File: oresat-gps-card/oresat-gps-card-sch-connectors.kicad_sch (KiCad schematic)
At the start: 27 parts, among them J1 J-SAMTEC-TFM-120-01-L-D-RA, J3 J-TE-Debug-2-1734592-0

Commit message: Updated schematic sheet links to match new naming
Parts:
- renumbered FID3 to FID?, FID4 to FID?, FID2 to FID?, FID5 to FID?, FID6 to FID?, FID1 to FID?, FLIGHT1 to FLIGHT?, PCB1 to PCB?
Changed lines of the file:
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@@
   (symbol (lib_id "oresat-graphics:FLIGHTMARKER") (at 152.4 238.76 0) (unit 1)
     (in_bom yes) (on_board yes) (fields_autoplaced)
-    (property "Reference" "FLIGHT1" (id 0) (at 152.4 238.76 0)
+    (property "Reference" "FLIGHT?" (id 0) (at 152.4 238.76 0)
       (effects (font (size 1.27 1.27)) hide)
     )
@@
   (symbol (lib_id "Mechanical:Fiducial") (at 165.1 248.92 0) (unit 1)
     (in_bom yes) (on_board yes)
-    (property "Reference" "FID3" (id 0) (at 163.83 252.73 0)
+    (property "Reference" "FID?" (id 0) (at 163.83 252.73 0)
       (effects (font (size 1.27 1.27)) (justify left) hide)
     )
@@
   (symbol (lib_id "Mechanical:Fiducial") (at 170.18 248.92 0) (unit 1)
     (in_bom yes) (on_board yes)
-    (property "Reference" "FID4" (id 0) (at 168.91 252.73 0)
+    (property "Reference" "FID?" (id 0) (at 168.91 252.73 0)
       (effects (font (size 1.27 1.27)) (justify left) hide)
     )
@@
   (symbol (lib_id "Mechanical:Fiducial") (at 160.02 248.92 0) (unit 1)
     (in_bom yes) (on_board yes)
-    (property "Reference" "FID2" (id 0) (at 158.75 252.73 0)
+    (property "Reference" "FID?" (id 0) (at 158.75 252.73 0)
       (effects (font (size 1.27 1.27)) (justify left) hide)
     )
@@
   (symbol (lib_id "Mechanical:Fiducial") (at 175.26 248.92 0) (unit 1)
     (in_bom yes) (on_board yes)
-    (property "Reference" "FID5" (id 0) (at 173.99 252.73 0)
+    (property "Reference" "FID?" (id 0) (at 173.99 252.73 0)
       (effects (font (size 1.27 1.27)) (justify left) hide)
     )
@@
   (symbol (lib_id "Mechanical:Fiducial") (at 180.34 248.92 0) (unit 1)
     (in_bom yes) (on_board yes)
-    (property "Reference" "FID6" (id 0) (at 179.07 252.73 0)
+    (property "Reference" "FID?" (id 0) (at 179.07 252.73 0)
       (effects (font (size 1.27 1.27)) (justify left) hide)
     )
@@
   (symbol (lib_id "OreSat-Cards:ORESAT-CARD-V1.3-GENERIC-1RF-POS2") (at 154.94 226.06 0) (unit 1)
     (in_bom no) (on_board yes) (fields_autoplaced)
-    (property "Reference" "PCB1" (id 0) (at 154.94 222.25 0)
+    (property "Reference" "PCB?" (id 0) (at 154.94 222.25 0)
       (effects (font (size 1.27 1.27)) hide)
     )
@@
   (symbol (lib_id "OreSat-Power:GND") (at 320.04 116.84 0) (unit 1)
     (in_bom yes) (on_board yes) (fields_autoplaced)
-    (property "Reference" "#GND0101" (id 0) (at 320.04 123.19 0)
+    (property "Reference" "#GND?" (id 0) (at 320.04 123.19 0)
       (effects (font (size 1.27 1.27)) hide)
     )
@@
   (symbol (lib_id "OreSat-Power:GND") (at 195.58 187.96 0) (unit 1)
     (in_bom yes) (on_board yes)
-    (property "Reference" "#GND0102" (id 0) (at 195.58 194.31 0)
+    (property "Reference" "#GND?" (id 0) (at 195.58 194.31 0)
       (effects (font (size 1.27 1.27)) hide)
     )
@@
   (symbol (lib_id "Mechanical:Fiducial") (at 154.94 248.92 0) (unit 1)
     (in_bom yes) (on_board yes)
-    (property "Reference" "FID1" (id 0) (at 153.67 252.73 0)
-      (effects (font (size 1.27 1.27)) (justify left) hide)
-    )
+    (property "Reference" "FID?" (id 0) (at 153.67 252.73 0)
+      (effects (font (size 1.27 1.27)) (justify left) hide)
+    )

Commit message: Quick GPS card design review changes
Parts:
- gave numbers to parts that had none: 8
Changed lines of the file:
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@@
   (symbol (lib_id "oresat-graphics:FLIGHTMARKER") (at 152.4 238.76 0) (unit 1)
     (in_bom yes) (on_board yes) (fields_autoplaced)
-    (property "Reference" "FLIGHT?" (id 0) (at 152.4 238.76 0)
+    (property "Reference" "FLIGHT1" (id 0) (at 152.4 238.76 0)
       (effects (font (size 1.27 1.27)) hide)
     )
@@
   (symbol (lib_id "Mechanical:Fiducial") (at 165.1 248.92 0) (unit 1)
     (in_bom yes) (on_board yes)
-    (property "Reference" "FID?" (id 0) (at 163.83 252.73 0)
+    (property "Reference" "FID3" (id 0) (at 163.83 252.73 0)
       (effects (font (size 1.27 1.27)) (justify left) hide)
     )
@@
   (symbol (lib_id "Mechanical:Fiducial") (at 170.18 248.92 0) (unit 1)
     (in_bom yes) (on_board yes)
-    (property "Reference" "FID?" (id 0) (at 168.91 252.73 0)
+    (property "Reference" "FID4" (id 0) (at 168.91 252.73 0)
       (effects (font (size 1.27 1.27)) (justify left) hide)
     )
@@
   (symbol (lib_id "Mechanical:Fiducial") (at 160.02 248.92 0) (unit 1)
     (in_bom yes) (on_board yes)
-    (property "Reference" "FID?" (id 0) (at 158.75 252.73 0)
+    (property "Reference" "FID2" (id 0) (at 158.75 252.73 0)
       (effects (font (size 1.27 1.27)) (justify left) hide)
     )
@@
   (symbol (lib_id "Mechanical:Fiducial") (at 175.26 248.92 0) (unit 1)
     (in_bom yes) (on_board yes)
-    (property "Reference" "FID?" (id 0) (at 173.99 252.73 0)
+    (property "Reference" "FID5" (id 0) (at 173.99 252.73 0)
       (effects (font (size 1.27 1.27)) (justify left) hide)
     )
@@
   (symbol (lib_id "Mechanical:Fiducial") (at 180.34 248.92 0) (unit 1)
     (in_bom yes) (on_board yes)
-    (property "Reference" "FID?" (id 0) (at 179.07 252.73 0)
+    (property "Reference" "FID6" (id 0) (at 179.07 252.73 0)
       (effects (font (size 1.27 1.27)) (justify left) hide)
     )
@@
   (symbol (lib_id "OreSat-Cards:ORESAT-CARD-V1.3-GENERIC-1RF-POS2") (at 154.94 226.06 0) (unit 1)
     (in_bom no) (on_board yes) (fields_autoplaced)
-    (property "Reference" "PCB?" (id 0) (at 154.94 222.25 0)
+    (property "Reference" "PCB1" (id 0) (at 154.94 222.25 0)
       (effects (font (size 1.27 1.27)) hide)
     )
@@
   (symbol (lib_id "OreSat-Power:GND") (at 320.04 116.84 0) (unit 1)
     (in_bom yes) (on_board yes) (fields_autoplaced)
-    (property "Reference" "#GND?" (id 0) (at 320.04 123.19 0)
+    (property "Reference" "#GND0101" (id 0) (at 320.04 123.19 0)
       (effects (font (size 1.27 1.27)) hide)
     )
@@
   (symbol (lib_id "OreSat-Power:GND") (at 195.58 187.96 0) (unit 1)
     (in_bom yes) (on_board yes)
-    (property "Reference" "#GND?" (id 0) (at 195.58 194.31 0)
+    (property "Reference" "#GND0102" (id 0) (at 195.58 194.31 0)
       (effects (font (size 1.27 1.27)) hide)
     )
@@
   (symbol (lib_id "Mechanical:Fiducial") (at 154.94 248.92 0) (unit 1)
     (in_bom yes) (on_board yes)
-    (property "Reference" "FID?" (id 0) (at 153.67 252.73 0)
-      (effects (font (size 1.27 1.27)) (justify left) hide)
-    )
+    (property "Reference" "FID1" (id 0) (at 153.67 252.73 0)
+      (effects (font (size 1.27 1.27)) (justify left) hide)
+    )

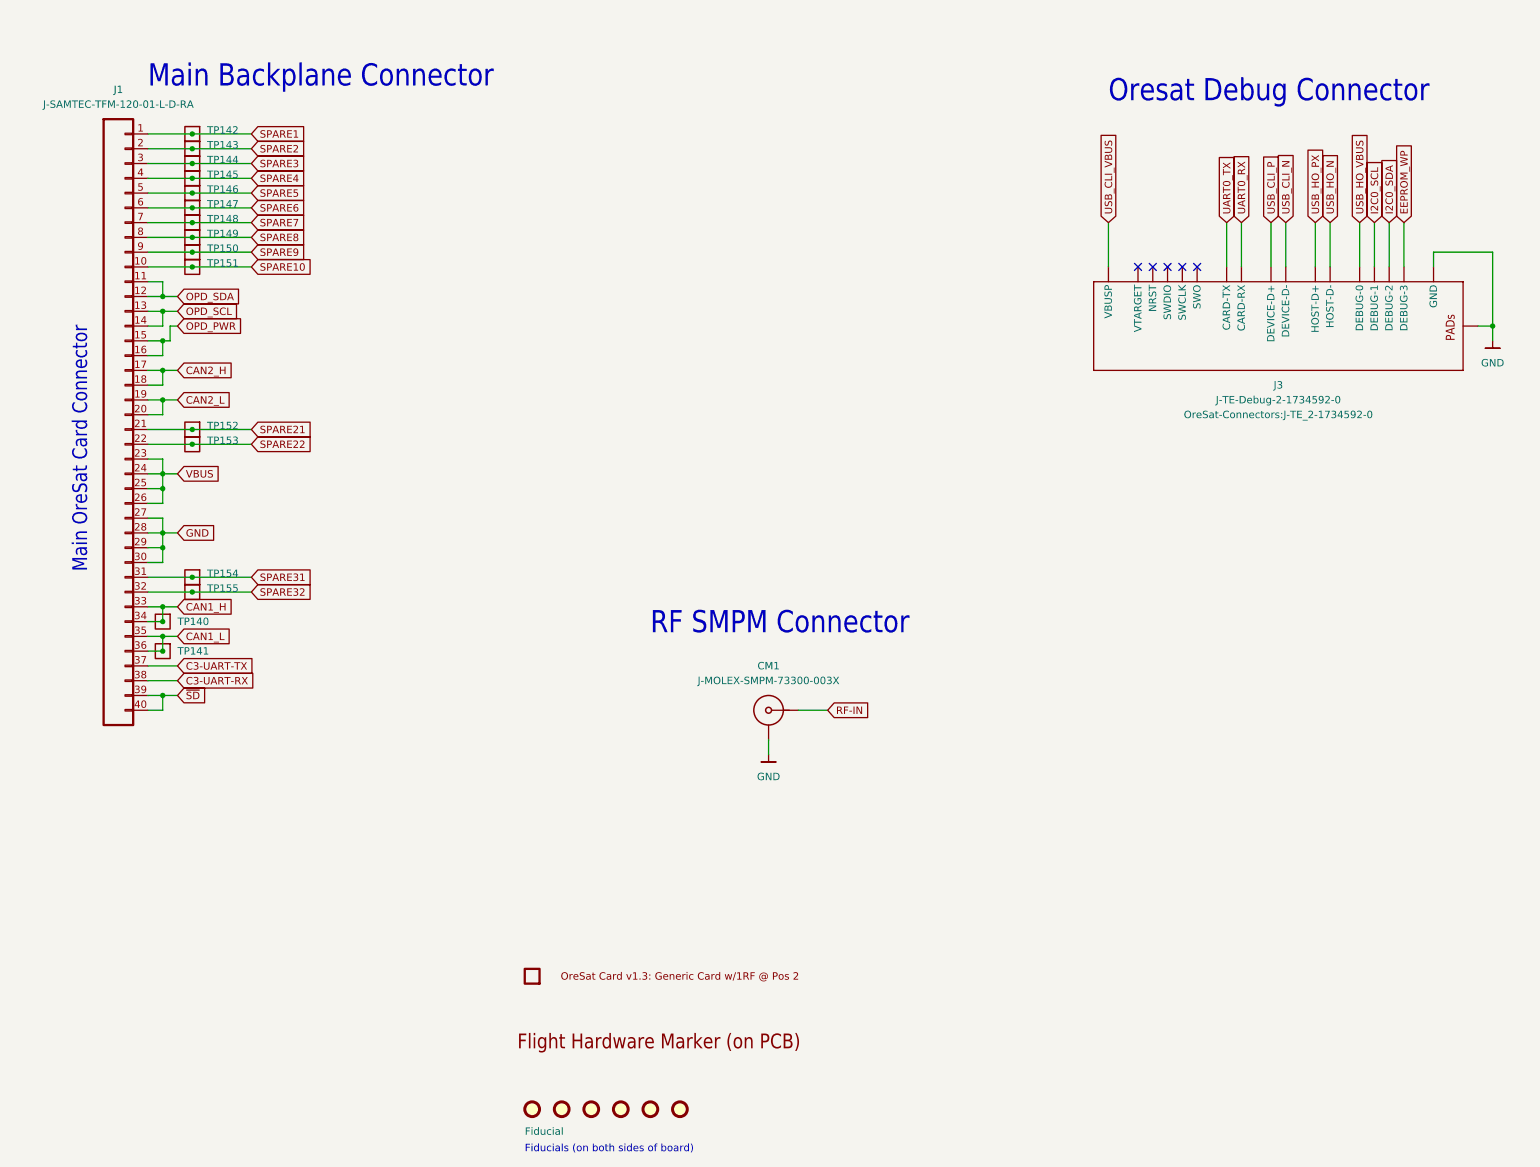
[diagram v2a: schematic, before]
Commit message: Updated GPS card with changes from C3 and notes. Fixed library issues
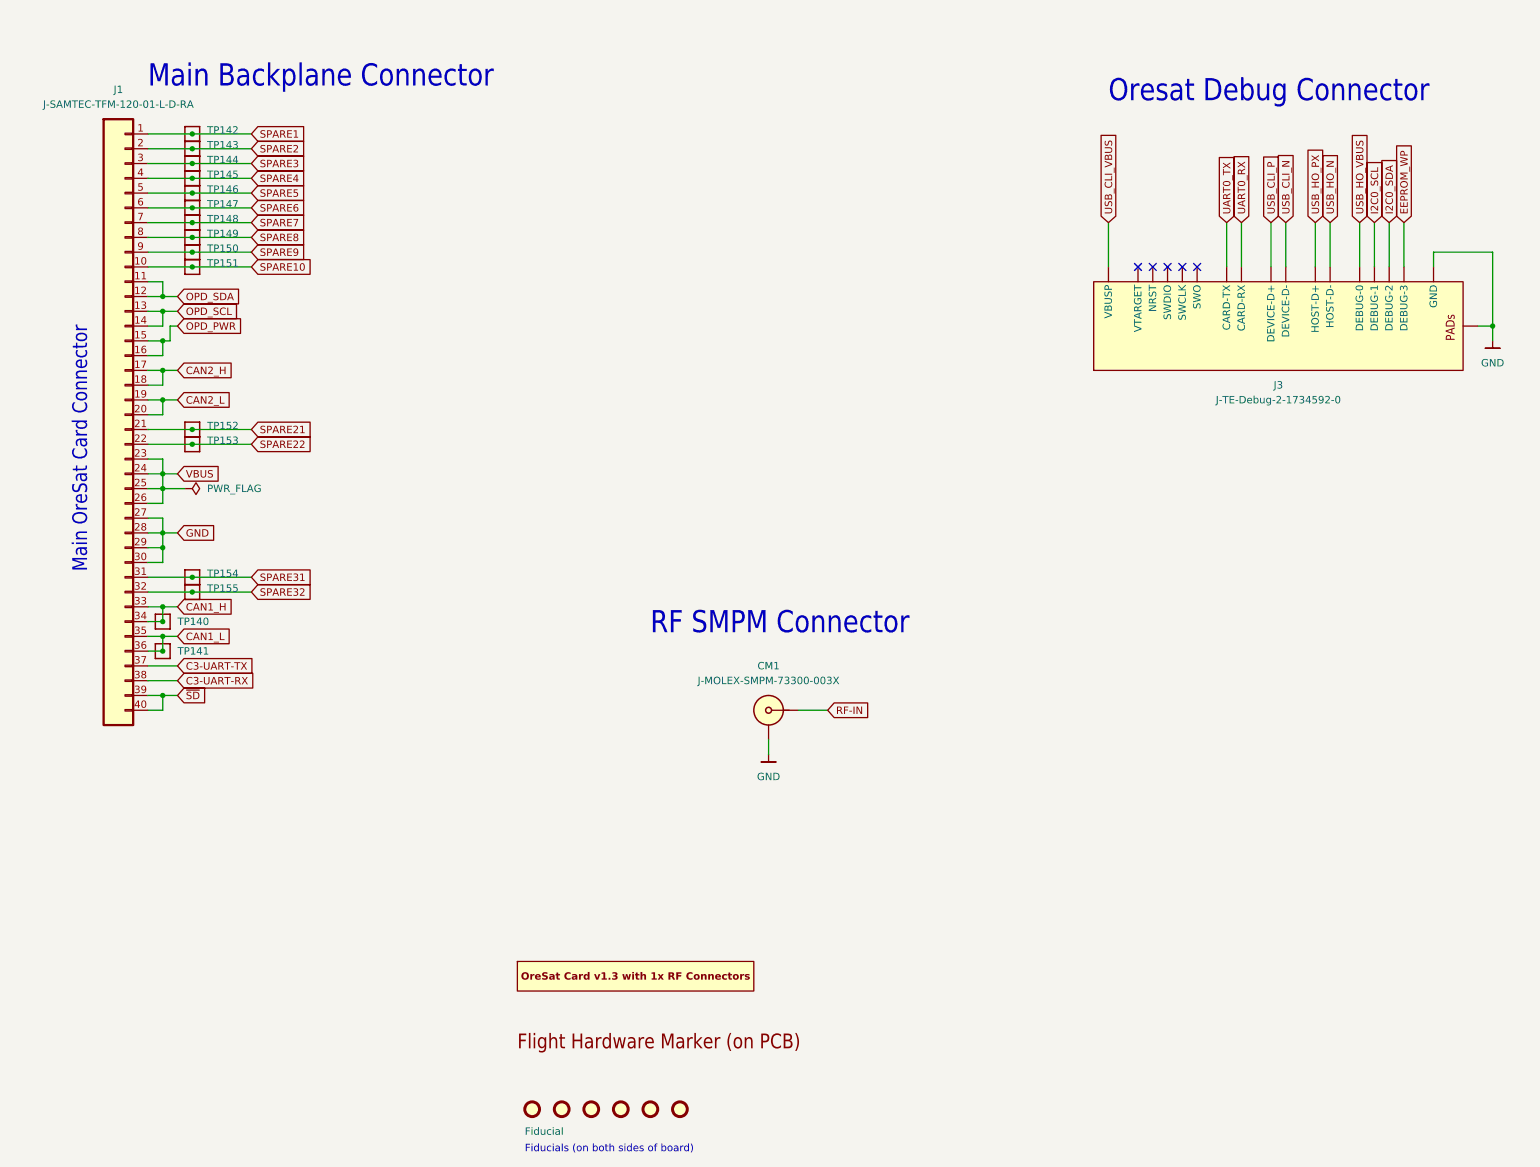
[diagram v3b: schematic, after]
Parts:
- CM1: footprint oresat-footprints:J-MOLEX-SMPM-073300-003X -> oresat-connectors:J-MOLEX-SMPM-073300-002X; symbol j-molex-smpm-73300-003x:J-MOLEX-SMPM-73300-003X -> oresat-connectors:J-MOLEX-SMPM-73300-002X
- J1: footprint OreSat-Connectors:J-SAMTEC-TFM-120-X1-XXX-D-RA -> oresat-connectors:J-SAMTEC-TFM-120-X1-XXX-D-RA; symbol OreSat-Connectors:J-SAMTEC-TFM-120-01-L-D-RA -> oresat-connectors:J-SAMTEC-TFM-120-01-L-D-RA
- J3: footprint OreSat-Connectors:J-TE_2-1734592-0 -> oresat-connectors:J-TE-2-1734592-0; symbol OreSat-Connectors:J-TE-Debug-2-1734592-0 -> oresat-connectors:J-TE-2-1734592-0
- PCB1: footprint OreSat-Cards:ORESAT-CARD-V1.3-GENERIC-1RF-POS2 -> oresat-pcbs:ORESAT-CARD-V1.3-2RF-RIGHT; symbol OreSat-Cards:ORESAT-CARD-V1.3-GENERIC-1RF-POS2 -> oresat-pcbs:ORESAT-CARD-V1.3-1RF-POS2; now in the parts list
- TP140, TP141, TP142, TP143, TP144, TP145, TP146, TP147, TP148, TP149, TP150, TP151, TP152, TP153, TP154, TP155: value Test-Point -> 0.03x0.04; footprint OreSat-TestPoint:PAD.03X.04 -> oresat-misc:TestPoint_Pad_D1.0mm; symbol OreSat-TestPoint:Test-Point -> oresat-misc:Test-Point-1mm-round
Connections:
- net GND: now also CM1.SHLD; no longer CM1.GND (SHIELD3)
- net RF-IN: now also CM1.SIG; no longer CM1.RF (CENTER)

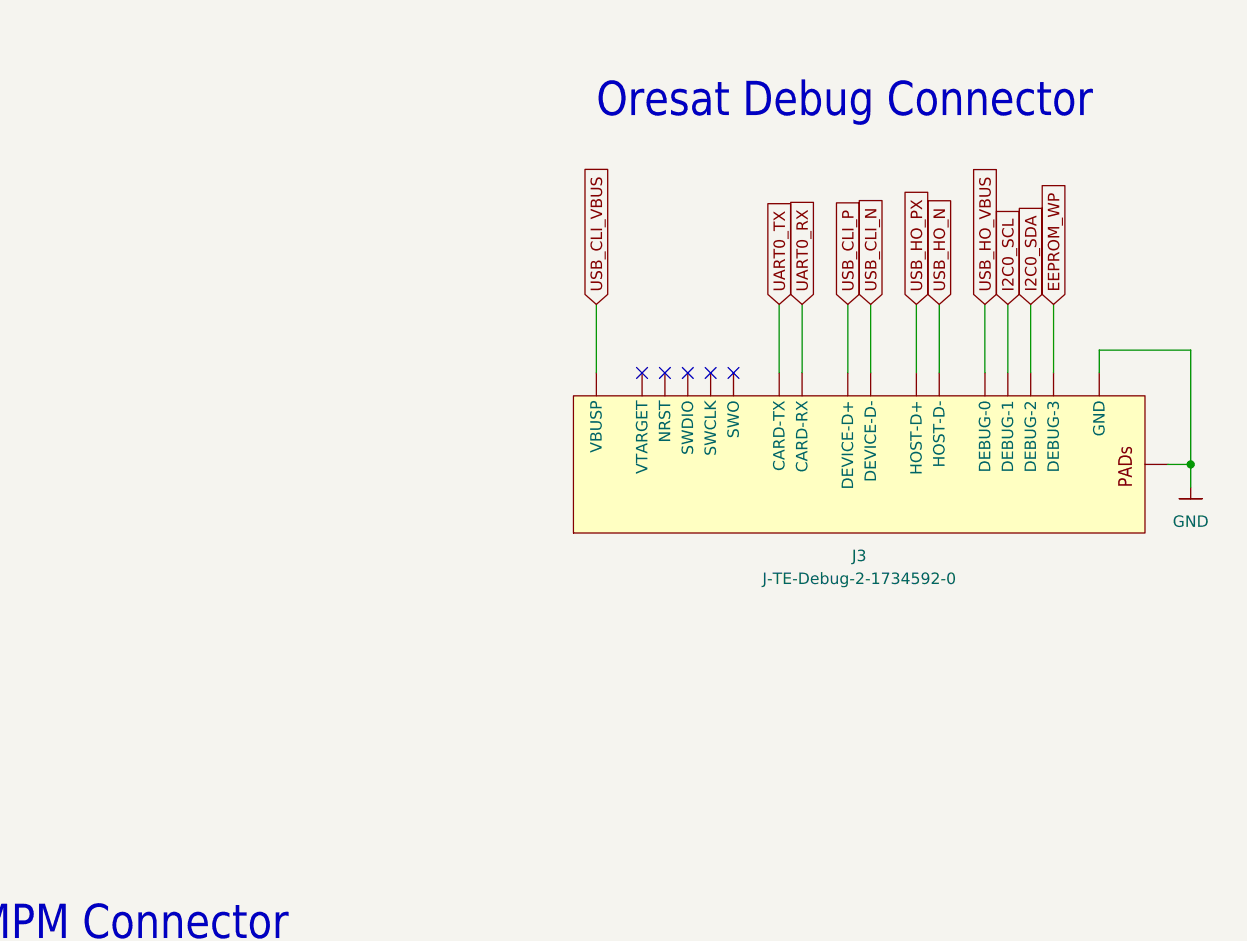
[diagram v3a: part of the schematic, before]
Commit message: Updated GPS card
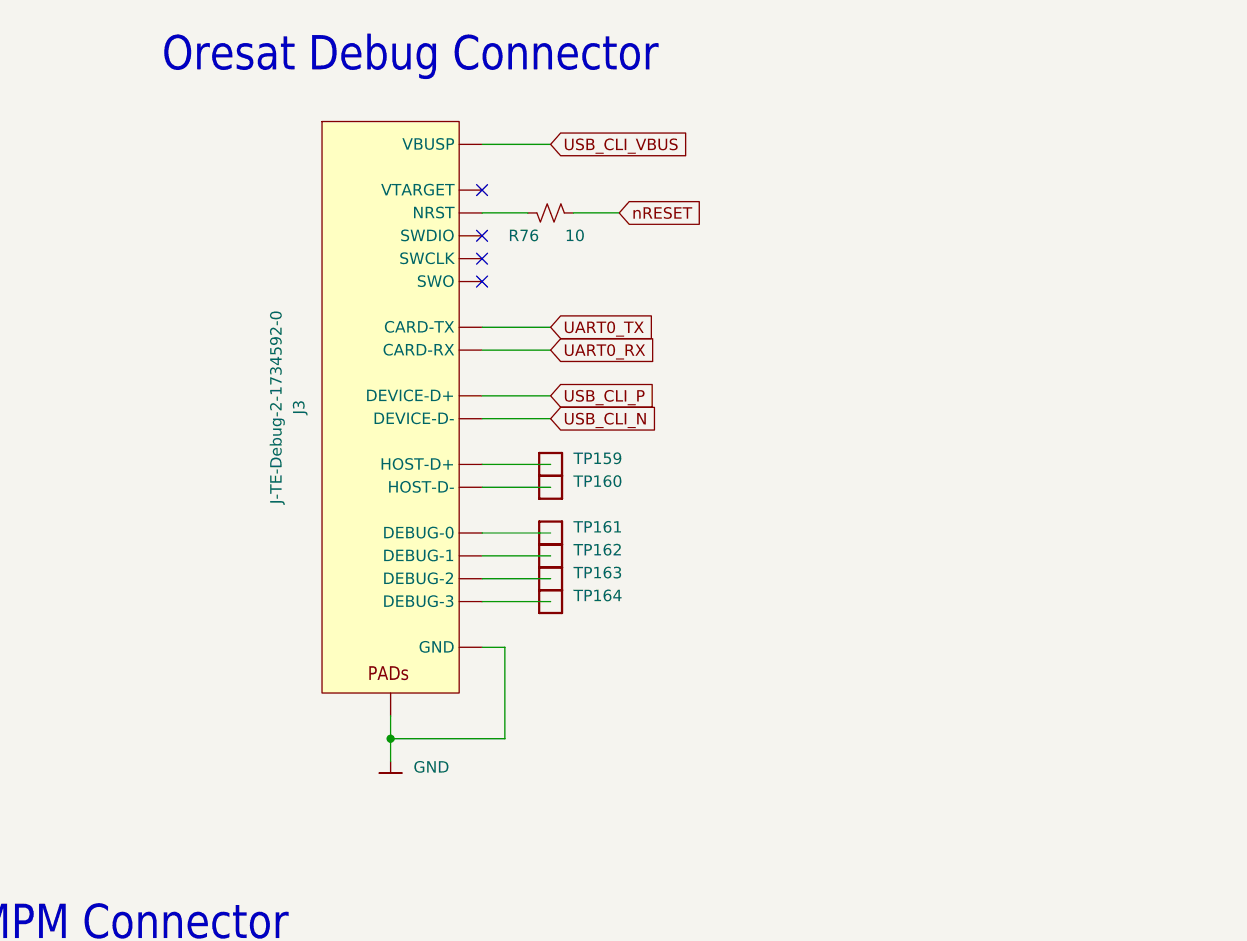
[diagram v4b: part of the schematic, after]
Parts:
- added R76: 10, Resistor_SMD:R_0603_1608Metric, symbol Device:R_Small_US
- added TP159, TP160, TP161, TP162, TP163, TP164: 0.03x0.04, oresat-misc:TestPoint_Pad_D1.0mm, symbol oresat-misc:Test-Point-1mm-round
- FID1, FID2, FID3, FID4, FID5, FID6: footprint oresat-misc:FIDUCIAL-1.0X2.0 -> Fiducial:Fiducial_1mm_Mask2mm
- PCB1: footprint oresat-pcbs:ORESAT-CARD-V1.3-2RF-RIGHT -> oresat-pcbs:ORESAT-CARD-V1.3-1RF-POS2
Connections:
- net at J3.10 (NRST): now also R76.1
- net EEPROM_WP: no longer names the net of J3.20 (DEBUG-3)
- net EEPROM_WP: now also TP164.1
- net I2C0_SCL: no longer names the net of J3.18 (DEBUG-1)
- net I2C0_SCL: now also TP162.1
- net I2C0_SDA: no longer names the net of J3.19 (DEBUG-2)
- net I2C0_SDA: now also TP163.1
- net USB_HO_N: no longer names the net of J3.8 (HOST-D-)
- net USB_HO_N: now also TP160.1
- net USB_HO_PX: no longer names the net of J3.7 (HOST-D+)
- net USB_HO_PX: now also TP159.1
- net USB_HO_VBUS: no longer names the net of J3.17 (DEBUG-0)
- net USB_HO_VBUS: now also TP161.1
- new net nRESET: R76.2
- no-connect marks 5 -> 4
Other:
- moved on the sheet: J3
